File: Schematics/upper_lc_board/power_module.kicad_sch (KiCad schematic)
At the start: 39 parts, among them J2 Stack Male Edge Connector, Q5 2N7002, U3 AMS1117-3.3, U4 ID_LM66100DCKR, U5 ID_LM66100DCKR, U9 DMP4065S-7

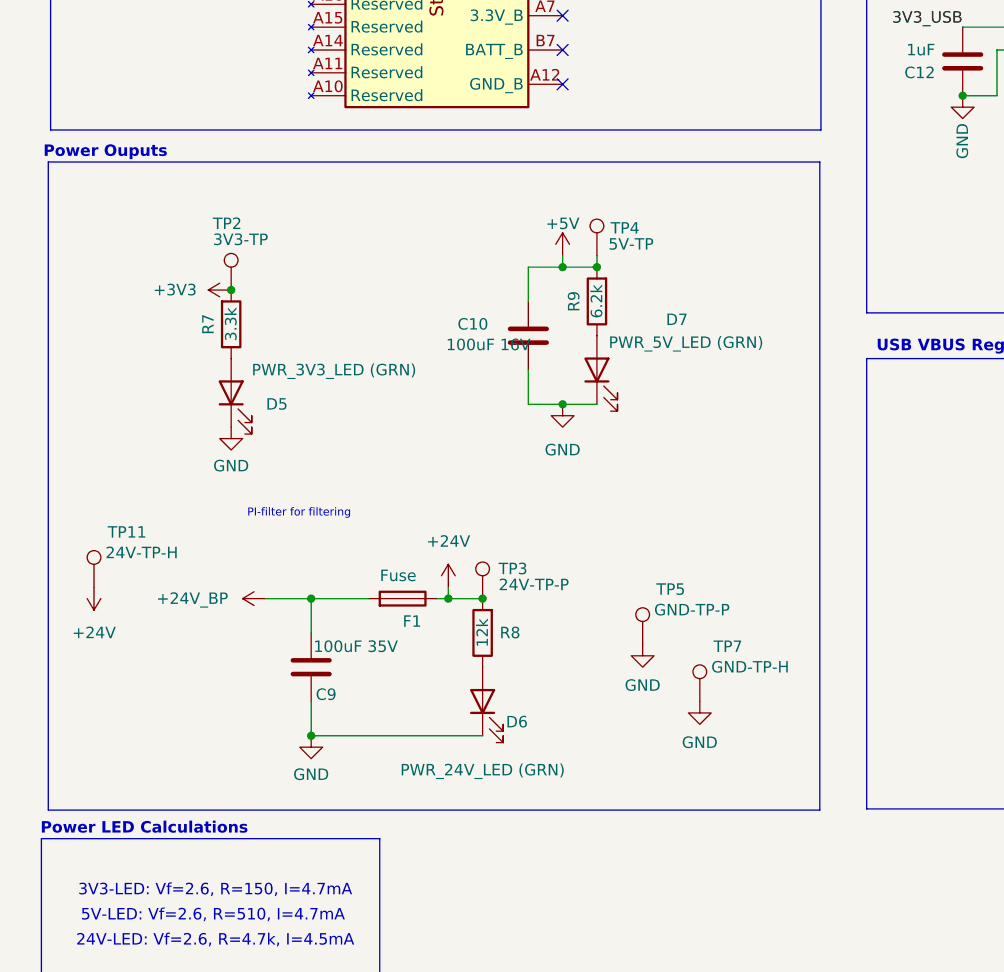
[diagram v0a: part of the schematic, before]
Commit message: added 24V sensing to upper board
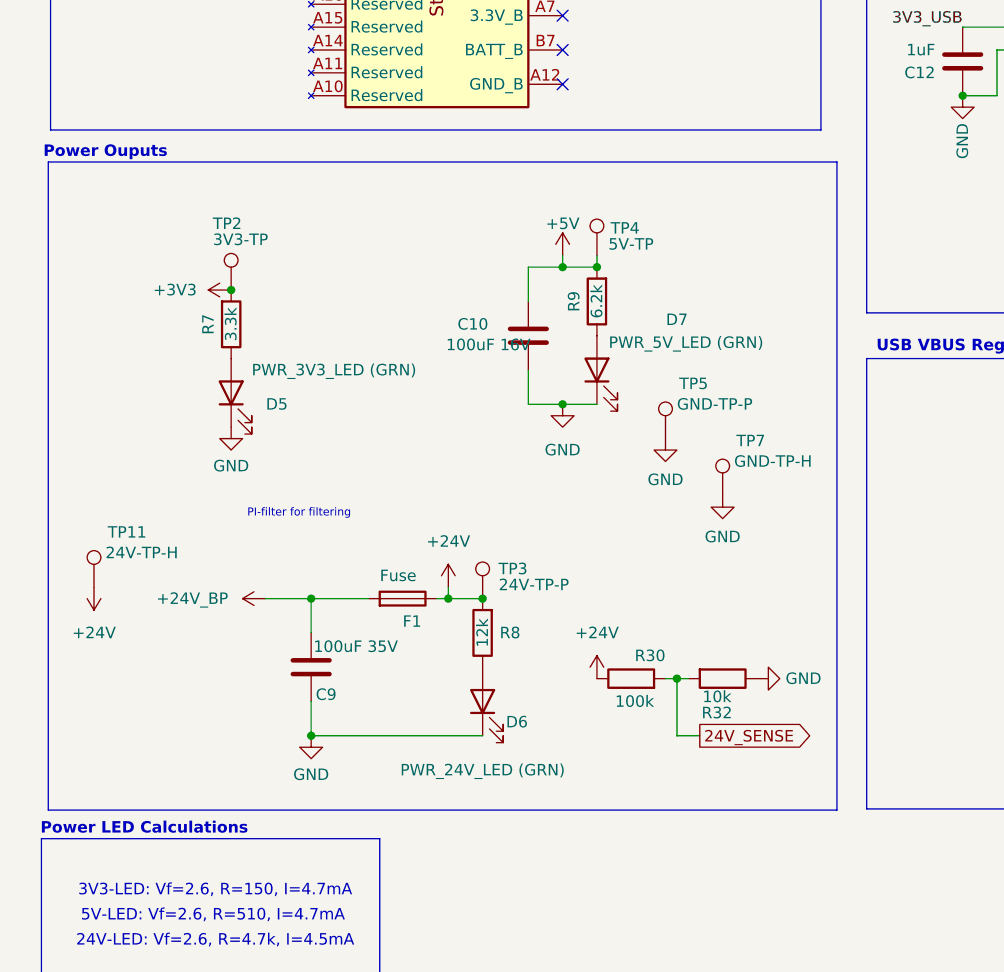
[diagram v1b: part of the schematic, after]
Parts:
- added R30: 100k, Resistor_SMD:R_0603_1608Metric, symbol Device:R
- added R32: 10k, Resistor_SMD:R_0603_1608Metric, symbol Device:R
- R8: footprint Resistor_SMD:R_1206_3216Metric_Pad1.30x1.75mm_HandSolder -> Resistor_SMD:R_0603_1608Metric; Digikey 311-12.1KFRCT-ND -> (none); LCSC C17912 -> C22790
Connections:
- net +24V: now also R30.1
- net GND: now also R32.1
- new net 24V_SENSE: R30.2, R32.2
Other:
- moved on the sheet: TP5, TP7

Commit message: add board-specifc READMEs (TODO), cleanup schematic titles
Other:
- title: Pegasus Power Circuitry -> Power Management Circuitry
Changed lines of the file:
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@@
 	(paper "A4")
 	(title_block
-		(title "Pegasus Power Circuitry")
+		(title "Power Management Circuitry")
 		(company "Queen's Rocket Engineering Team")
-		(comment 1 "Upper Control Board V2")
-		(comment 2 "Jeevan Sanchez")
+		(comment 1 "Contributors: Jeevan Sanchez, Tristan Alderson")
+		(comment 2 "PEGASUS - Upper Control Board")
 	)
 	(junction
@@
 	(rectangle
 		(start 196.85 27.94)
-		(end 266.7 77.47)
+		(end 271.78 77.47)
 		(stroke
 			(width 0)
@@
 		(dnp no)
 		(property "Reference" "C24"
-			(at 259.842 65.532 0)
+			(at 266.446 67.31 0)
 			(effects
 				(font
@@
 		)
 		(property "Value" "0.1uF"
-			(at 264.668 65.278 0)
+			(at 266.954 69.596 0)
 			(effects
 				(font

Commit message: add ed pinouts
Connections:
- net VPT-SW renamed VPT_EN
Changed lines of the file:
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@@
 		)
 	)
-	(global_label "VPT-SW"
+	(global_label "VPT_EN"
 		(shape input)
 		(at 232.41 45.72 0)
@@
 		)
 		(property "Intersheetrefs" "${INTERSHEET_REFS}"
-			(at 242.9547 45.72 0)
+			(at 242.1685 45.72 0)
 			(effects
 				(font
